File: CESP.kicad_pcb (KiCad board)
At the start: 2 copper layers, 50.8 x 25.4 mm, 0 parts

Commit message: third commit
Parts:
- added C1: C, SM0805, F.Cu at (160.0, 148.6)
- added C2: C, SM0805, F.Cu at (160.0, 144.0)
- added C3: C, SM0603, F.Cu at (160.0, 139.7)
- added R1: R, R3, F.Cu at (156.2, 146.1)
- added R2: R, R3, F.Cu at (156.2, 135.9)
- added R3: R, R1, F.Cu at (160.0, 133.3)
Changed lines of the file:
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@@
 (kicad_pcb (version 3) (host pcbnew "(2014-01-10 BZR 4027)-stable")
   (general
-    (links 0)
-    (no_connects 0)
-    (area 155.880999 95.682999 211.911001 140.537001)
+    (links 6)
+    (no_connects 6)
+    (area 152.324999 126.924999 203.275001 152.475001)
     (thickness 1.6)
     (drawings 4)
     (tracks 0)
     (zones 0)
-    (modules 0)
-    (nets 1)
+    (modules 6)
+    (nets 7)
   )
   (page A3)
@@
   )
   (net 0 "")
+  (net 1 +5V)
+  (net 2 GND)
+  (net 3 N-000003)
+  (net 4 N-000004)
+  (net 5 N-000005)
+  (net 6 N-000006)
   (net_class Default "This is the default net class."
     (clearance 0.254)
@@
     (uvia_drill 0.127)
     (add_net "")
+    (add_net +5V)
+    (add_net GND)
+    (add_net N-000003)
+    (add_net N-000004)
+    (add_net N-000005)
+    (add_net N-000006)
+  )
+  (module SM0805 (layer F.Cu)
+    (at 160.02 148.59 90)
+    (attr smd)
+    (fp_text reference C1 (at 0 -0.3175 90) (layer F.SilkS)
+      (effects (font (size 0.50038 0.50038) (thickness 0.10922)))
+    )
+    (fp_text value C (at 0 0.381 90) (layer F.SilkS)
+      (effects (font (size 0.50038 0.50038) (thickness 0.10922)))
+    )
+    (fp_circle (center -1.651 0.762) (end -1.651 0.635) (layer F.SilkS) (width 0.09906))
+    (fp_line (start -0.508 0.762) (end -1.524 0.762) (layer F.SilkS) (width 0.09906))
+    (fp_line (start -1.524 0.762) (end -1.524 -0.762) (layer F.SilkS) (width 0.09906))
+    (fp_line (start -1.524 -0.762) (end -0.508 -0.762) (layer F.SilkS) (width 0.09906))
+    (fp_line (start 0.508 -0.762) (end 1.524 -0.762) (layer F.SilkS) (width 0.09906))
+    (fp_line (start 1.524 -0.762) (end 1.524 0.762) (layer F.SilkS) (width 0.09906))
+    (fp_line (start 1.524 0.762) (end 0.508 0.762) (layer F.SilkS) (width 0.09906))
+    (pad 1 smd rect (at -0.9525 0 90) (size 0.889 1.397)
+      (layers F.Cu F.Paste F.Mask)
+      (net 1 +5V)
+    )
+    (pad 2 smd rect (at 0.9525 0 90) (size 0.889 1.397)
+      (layers F.Cu F.Paste F.Mask)
+      (net 4 N-000004)
+    )
+    (model smd/chip_cms.wrl
+      (at (xyz 0 0 0))
+      (scale (xyz 0.1 0.1 0.1))
+      (rotate (xyz 0 0 0))
+    )
+  )
+  (module SM0805 (layer F.Cu)
+    (at 160.02 144.018 90)
+    (attr smd)
+    (fp_text reference C2 (at 0 -0.3175 90) (layer F.SilkS)
+      (effects (font (size 0.50038 0.50038) (thickness 0.10922)))
+    )
+    (fp_text value C (at 0 0.381 90) (layer F.SilkS)
+      (effects (font (size 0.50038 0.50038) (thickness 0.10922)))
+    )
+    (fp_circle (center -1.651 0.762) (end -1.651 0.635) (layer F.SilkS) (width 0.09906))
+    (fp_line (start -0.508 0.762) (end -1.524 0.762) (layer F.SilkS) (width 0.09906))
+    (fp_line (start -1.524 0.762) (end -1.524 -0.762) (layer F.SilkS) (width 0.09906))
+    (fp_line (start -1.524 -0.762) (end -0.508 -0.762) (layer F.SilkS) (width 0.09906))
+    (fp_line (start 0.508 -0.762) (end 1.524 -0.762) (layer F.SilkS) (width 0.09906))
+    (fp_line (start 1.524 -0.762) (end 1.524 0.762) (layer F.SilkS) (width 0.09906))
+    (fp_line (start 1.524 0.762) (end 0.508 0.762) (layer F.SilkS) (width 0.09906))
+    (pad 1 smd rect (at -0.9525 0 90) (size 0.889 1.397)
+      (layers F.Cu F.Paste F.Mask)
+      (net 4 N-000004)
+    )
+    (pad 2 smd rect (at 0.9525 0 90) (size 0.889 1.397)
+      (layers F.Cu F.Paste F.Mask)
+      (net 3 N-000003)
+    )
+    (model smd/chip_cms.wrl
+      (at (xyz 0 0 0))
+      (scale (xyz 0.1 0.1 0.1))
+      (rotate (xyz 0 0 0))
+    )
+  )
+  (module SM0603 (layer F.Cu)
+    (at 160.02 139.7 90)
+    (attr smd)
+    (fp_text reference C3 (at 0 0 90) (layer F.SilkS)
+      (effects (font (size 0.508 0.4572) (thickness 0.1143)))
+    )
+    (fp_text value C (at 0 0 90) (layer F.SilkS) hide
+      (effects (font (size 0.508 0.4572) (thickness 0.1143)))
+    )
+    (fp_line (start -1.143 -0.635) (end 1.143 -0.635) (layer F.SilkS) (width 0.127))
+    (fp_line (start 1.143 -0.635) (end 1.143 0.635) (layer F.SilkS) (width 0.127))
+    (fp_line (start 1.143 0.635) (end -1.143 0.635) (layer F.SilkS) (width 0.127))
+    (fp_line (start -1.143 0.635) (end -1.143 -0.635) (layer F.SilkS) (width 0.127))
+    (pad 1 smd rect (at -0.762 0 90) (size 0.635 1.143)
+      (layers F.Cu F.Paste F.Mask)
+      (net 3 N-000003)
+    )
+    (pad 2 smd rect (at 0.762 0 90) (size 0.635 1.143)
+      (layers F.Cu F.Paste F.Mask)
+      (net 2 GND)
+    )
+    (model smd\resistors\R0603.wrl
+      (at (xyz 0 0 0.001))
+      (scale (xyz 0.5 0.5 0.5))
+      (rotate (xyz 0 0 0))
+    )
+  )
+  (module R3 (layer F.Cu)
+    (at 156.21 146.05 90)
+    (descr "Resitance 3 pas")
+    (tags R)
+    (autoplace_cost180 10)
+    (fp_text reference R1 (at 0 0.127 90) (layer F.SilkS) hide
+      (effects (font (size 1.397 1.27) (thickness 0.2032)))
+    )
+    (fp_text value R (at 0 0.127 90) (layer F.SilkS)
+      (effects (font (size 1.397 1.27) (thickness 0.2032)))
+    )
+    (fp_line (start -3.81 0) (end -3.302 0) (layer F.SilkS) (width 0.2032))
+    (fp_line (start 3.81 0) (end 3.302 0) (layer F.SilkS) (width 0.2032))
+    (fp_line (start 3.302 0) (end 3.302 -1.016) (layer F.SilkS) (width 0.2032))
+    (fp_line (start 3.302 -1.016) (end -3.302 -1.016) (layer F.SilkS) (width 0.2032))
+    (fp_line (start -3.302 -1.016) (end -3.302 1.016) (layer F.SilkS) (width 0.2032))
+    (fp_line (start -3.302 1.016) (end 3.302 1.016) (layer F.SilkS) (width 0.2032))
+    (fp_line (start 3.302 1.016) (end 3.302 0) (layer F.SilkS) (width 0.2032))
+    (fp_line (start -3.302 -0.508) (end -2.794 -1.016) (layer F.SilkS) (width 0.2032))
+    (pad 1 thru_hole circle (at -3.81 0 90) (size 1.397 1.397) (drill 0.8128)
+      (layers *.Cu *.Mask F.SilkS)
+      (net 1 +5V)
+    )
+    (pad 2 thru_hole circle (at 3.81 0 90) (size 1.397 1.397) (drill 0.8128)
+      (layers *.Cu *.Mask F.SilkS)
+      (net 6 N-000006)
+    )
+    (model discret/resistor.wrl
+      (at (xyz 0 0 0))
+      (scale (xyz 0.3 0.3 0.3))
+      (rotate (xyz 0 0 0))
+    )
+  )
+  (module R3 (layer F.Cu)
+    (at 156.21 135.89 90)
+    (descr "Resitance 3 pas")
+    (tags R)
+    (autoplace_cost180 10)
+    (fp_text reference R2 (at 0 0.127 90) (layer F.SilkS) hide
+      (effects (font (size 1.397 1.27) (thickness 0.2032)))
+    )
+    (fp_text value R (at 0 0.127 90) (layer F.SilkS)
+      (effects (font (size 1.397 1.27) (thickness 0.2032)))
+    )
+    (fp_line (start -3.81 0) (end -3.302 0) (layer F.SilkS) (width 0.2032))
+    (fp_line (start 3.81 0) (end 3.302 0) (layer F.SilkS) (width 0.2032))
+    (fp_line (start 3.302 0) (end 3.302 -1.016) (layer F.SilkS) (width 0.2032))
+    (fp_line (start 3.302 -1.016) (end -3.302 -1.016) (layer F.SilkS) (width 0.2032))
+    (fp_line (start -3.302 -1.016) (end -3.302 1.016) (layer F.SilkS) (width 0.2032))
+    (fp_line (start -3.302 1.016) (end 3.302 1.016) (layer F.SilkS) (width 0.2032))
+    (fp_line (start 3.302 1.016) (end 3.302 0) (layer F.SilkS) (width 0.2032))
+    (fp_line (start -3.302 -0.508) (end -2.794 -1.016) (layer F.SilkS) (width 0.2032))
+    (pad 1 thru_hole circle (at -3.81 0 90) (size 1.397 1.397) (drill 0.8128)
+      (layers *.Cu *.Mask F.SilkS)
+      (net 6 N-000006)
+    )
+    (pad 2 thru_hole circle (at 3.81 0 90) (size 1.397 1.397) (drill 0.8128)
+      (layers *.Cu *.Mask F.SilkS)
+      (net 5 N-000005)
+    )
+    (model discret/resistor.wrl
+      (at (xyz 0 0 0))
+      (scale (xyz 0.3 0.3 0.3))
+      (rotate (xyz 0 0 0))
+    )
+  )
+  (module R1 (layer F.Cu)
+    (at 160.02 133.35 90)
+    (descr "Resistance verticale")
+    (tags R)
+    (autoplace_cost90 10)
+    (autoplace_cost180 10)
+    (fp_text reference R3 (at -1.016 2.54 90) (layer F.SilkS)
+      (effects (font (size 1.397 1.27) (thickness 0.2032)))
+    )
+    (fp_text value R (at -1.143 2.54 90) (layer F.SilkS) hide
+      (effects (font (size 1.397 1.27) (thickness 0.2032)))
+    )
+    (fp_line (start -1.27 0) (end 1.27 0) (layer F.SilkS) (width 0.381))
+    (fp_circle (center -1.27 0) (end -0.635 1.27) (layer F.SilkS) (width 0.381))
+    (pad 1 thru_hole circle (at -1.27 0 90) (size 1.397 1.397) (drill 0.8128)
+      (layers *.Cu *.Mask F.SilkS)
+      (net 2 GND)
+    )
+    (pad 2 thru_hole circle (at 1.27 0 90) (size 1.397 1.397) (drill 0.8128)
+      (layers *.Cu *.Mask F.SilkS)
+      (net 5 N-000005)
+    )
+    (model discret/verti_resistor.wrl
+      (at (xyz 0 0 0))
+      (scale (xyz 1 1 1))
+      (rotate (xyz 0 0 0))
+    )
   )
   (gr_line (start 152.4 127) (end 152.4 152.4) (angle 90) (layer Edge.Cuts) (width 0.15))

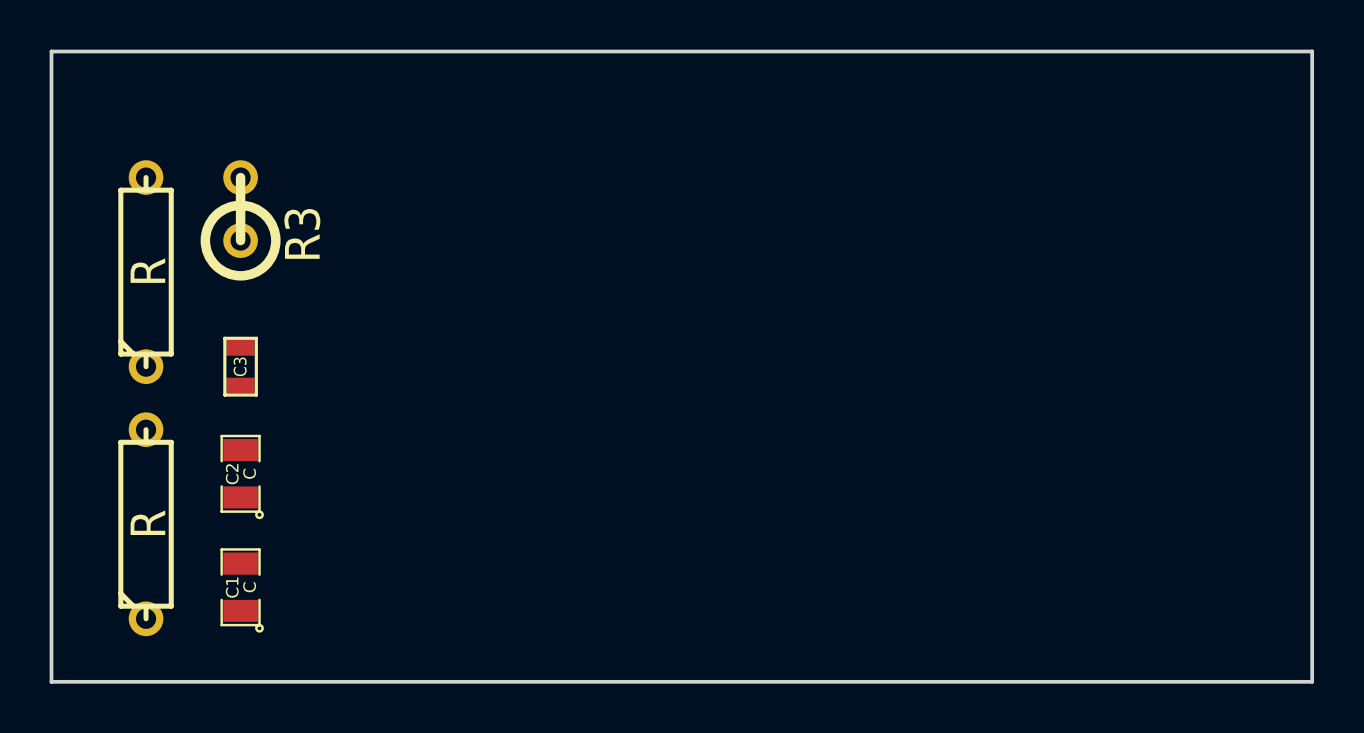
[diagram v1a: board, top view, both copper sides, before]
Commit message: Added SPIvsSPI Library
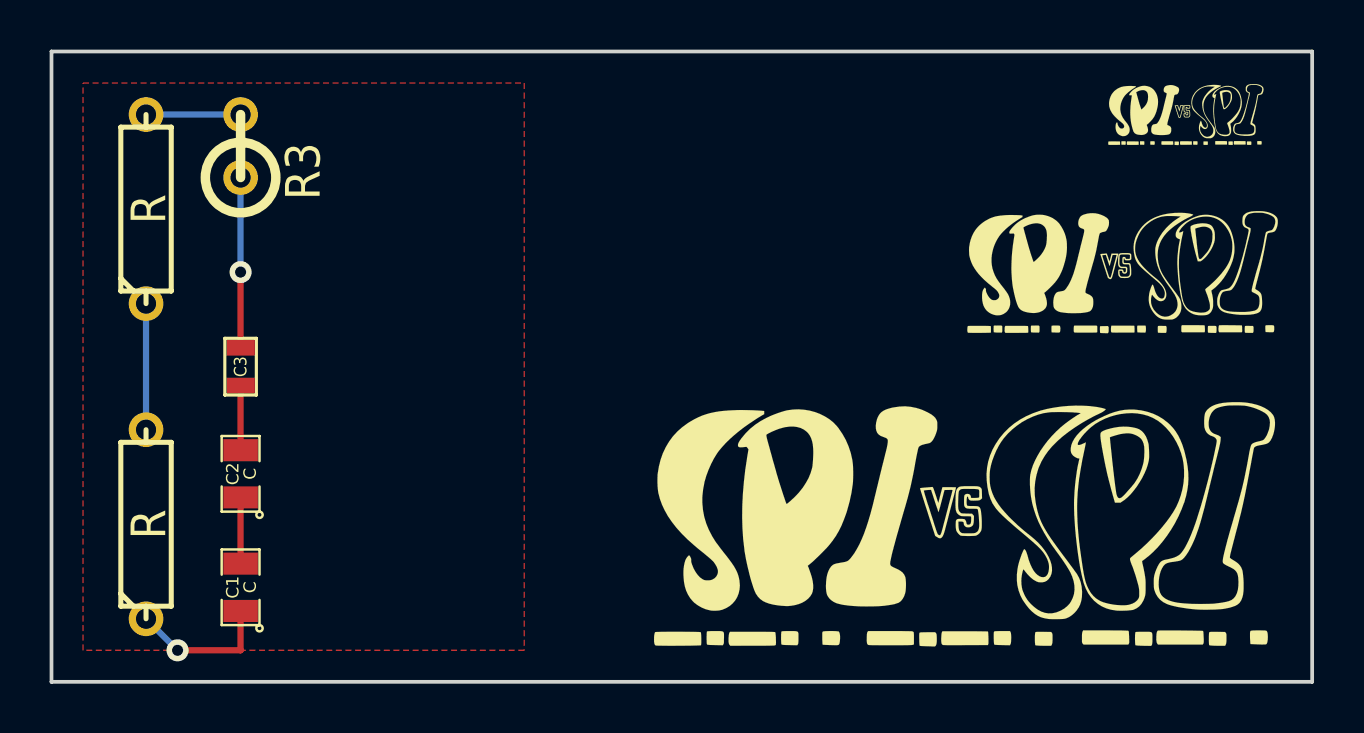
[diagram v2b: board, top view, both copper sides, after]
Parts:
- added VAL: SPIvsSPI_250, SPIvsSPI_250, F.Cu at (198.1, 129.5)
- added VAL: SPIvsSPI_1, SPIvsSPI_500, F.Cu at (195.6, 135.9)
- added VAL: SPIvsSPI_1, SPIvsSPI_1000, F.Cu at (189.2, 146.1)
- moved R2 2.54 mm to (156.2, 133.3)
- moved R3 2.54 mm to (160.0, 130.8)
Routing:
- net GND: track 0.00 -> 6.86 mm, vias 0 -> 1
- net +5V: track 0.00 -> 5.92 mm, vias 0 -> 1
- net N-000006: track 0.00 -> 5.08 mm
- net N-000005: track 0.00 -> 3.81 mm
- net N-000004: track 0.00 -> 2.67 mm
- net N-000003: track 0.00 -> 2.60 mm
- added copper zone on F.Cu, net GND
